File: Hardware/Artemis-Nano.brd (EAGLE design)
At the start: 43.2 x 20.3 mm, 129 parts, among them J10 USB-C, J11 CORTEX_DEBUG, U2 MCP73831, U3 3.3V, U4 ARTEMIS_MODULESMD, U6 CH340E_MSOP10, Y2 32.768kHz

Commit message: Rename to Nano. Add ignore. Add panel.
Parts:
- removed LOGO2: OSHW-LOGOS, SparkFun-Aesthetics:OSHW-LOGO-S
- removed LOGO3: SFE_LOGO_NAME_FLAME.1_INCH, SparkFun-Aesthetics:SFE_LOGO_NAME_FLAME_.1
- added U$25: (no value), SparkFun-Aesthetics:PRODUCTION_INSTRUCTIONS
- moved FRAME2 55.3 mm to (0.00, 0.00)
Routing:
- net 3.3V: track 50.7 -> 46.9 mm
- net GND: track 31.5 -> 28.7 mm
- added copper zone on layer 15, net 3.3V
- added copper zone on layer 2, net GND
- removed copper zone on layer 2, net 3.3V
- removed copper zone on layer 15, net GND
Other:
- board text added: "0.8mm Thickness"
- board text added: "Four-layer board"

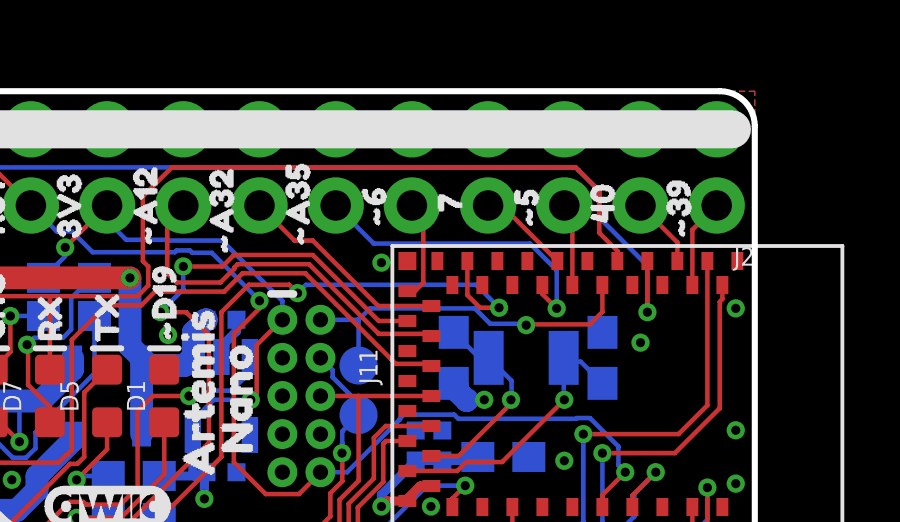
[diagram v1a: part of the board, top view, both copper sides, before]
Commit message: Fixing PWM pin 7. Updating schematic symbol.
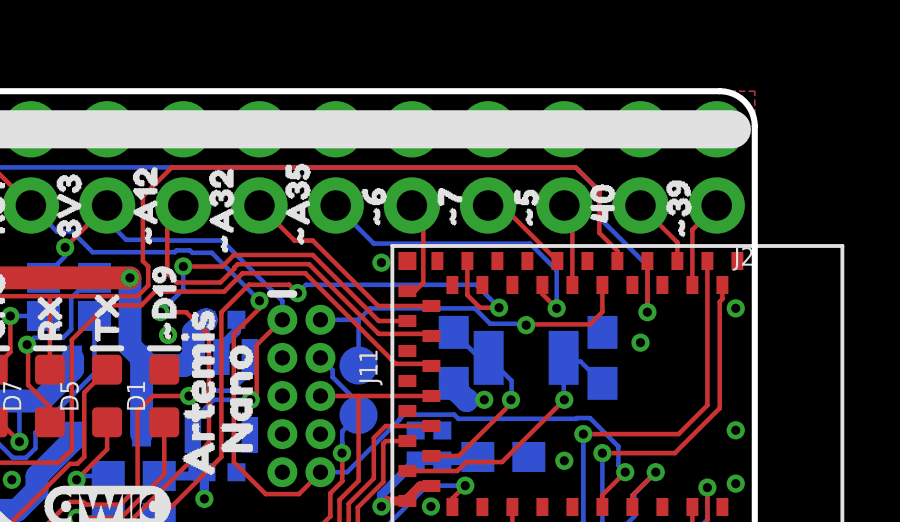
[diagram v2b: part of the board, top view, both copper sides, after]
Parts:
- removed U$20, U$79: (no value), buzzard_labels (10):78
- added U$32, U$34: (no value), buzzard_labels (1):#71
- moved U$19 0.25 mm to (36.2, 15.4)
- renumbered U4 to U1
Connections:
- net D7/MOSI renamed ~D7/MOSI

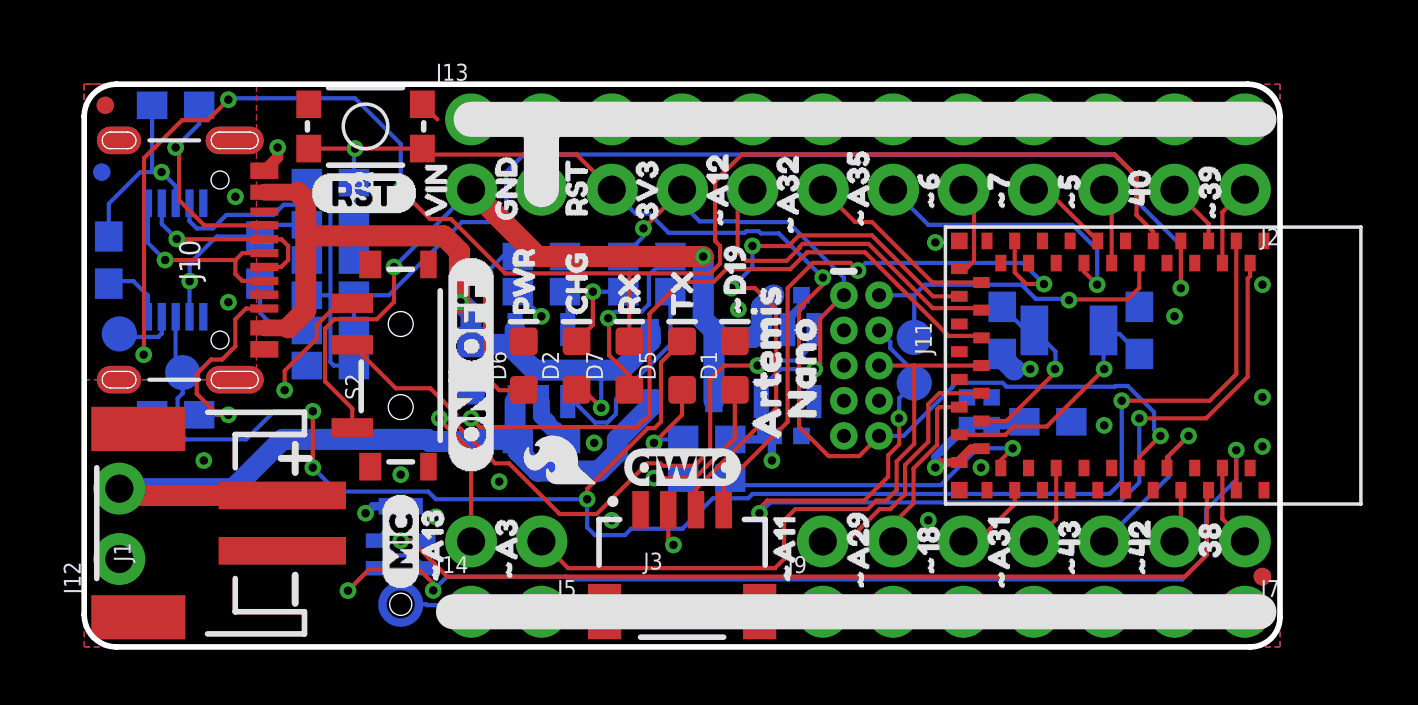
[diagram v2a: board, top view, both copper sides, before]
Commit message: Fix pin 33 silk
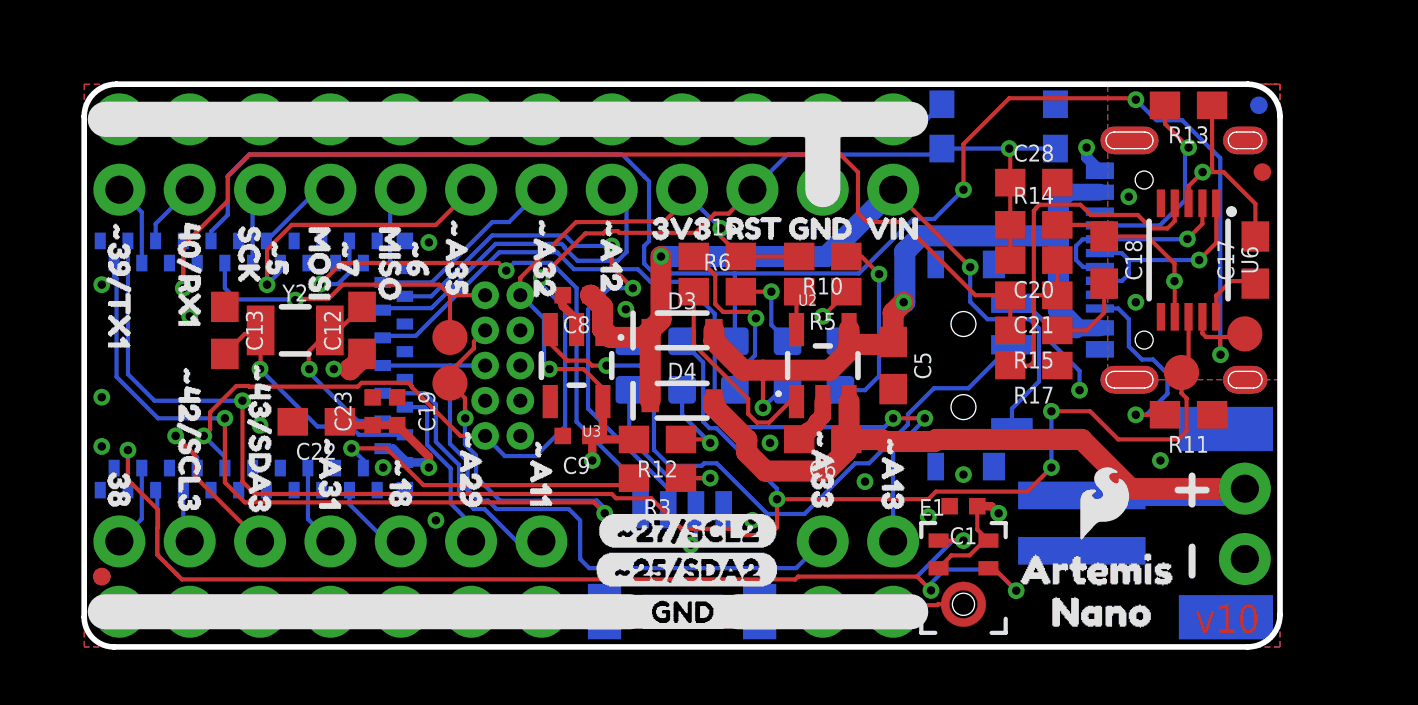
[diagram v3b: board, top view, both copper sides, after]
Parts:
- removed U$69, U$70: (no value), buzzard_labels (10):#A320
- added U$20, U$36: (no value), buzzard_labels (4):#A331
- moved U$25 55.9 mm to (-6.35, 50.8), flipped to the bottom
- moved FRAME2 43.2 mm to (43.2, 0.00), flipped to the top
- moved FD1 41.9 mm to (0.64, 2.54), flipped to the bottom
- moved FD3 41.9 mm to (42.5, 17.1), flipped to the top
- moved FD4 41.9 mm to (0.64, 2.54), flipped to the top
- moved FD2 41.7 mm to (42.4, 19.6), flipped to the bottom
- moved C17 41.4 mm to (42.3, 14.0), flipped to the top
- moved J12 40.6 mm to (41.9, 3.17), flipped to the bottom
- moved J2 40.6 mm to (1.27, 16.5), flipped to the bottom
- moved J7 40.6 mm to (1.27, 3.81), flipped to the bottom
- moved TP6 40.6 mm to (41.9, 11.3), flipped to the top
- moved U$31 40.6 mm to (1.27, 6.99), flipped to the top
- moved U$48 40.6 mm to (1.27, 16.0), flipped to the top
- moved FRAME1 38.1 mm to (40.6, -21.6), flipped to the bottom
- moved U$62 38.1 mm to (2.54, 14.7), flipped to the bottom
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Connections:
- net ~AD3/SWO renamed ~AD33/SWO
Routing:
- net PDMDATA: track 33.2 -> 6.59 mm
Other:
- outline, holes or cut-outs redrawn

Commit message: Fix pin 33 silk
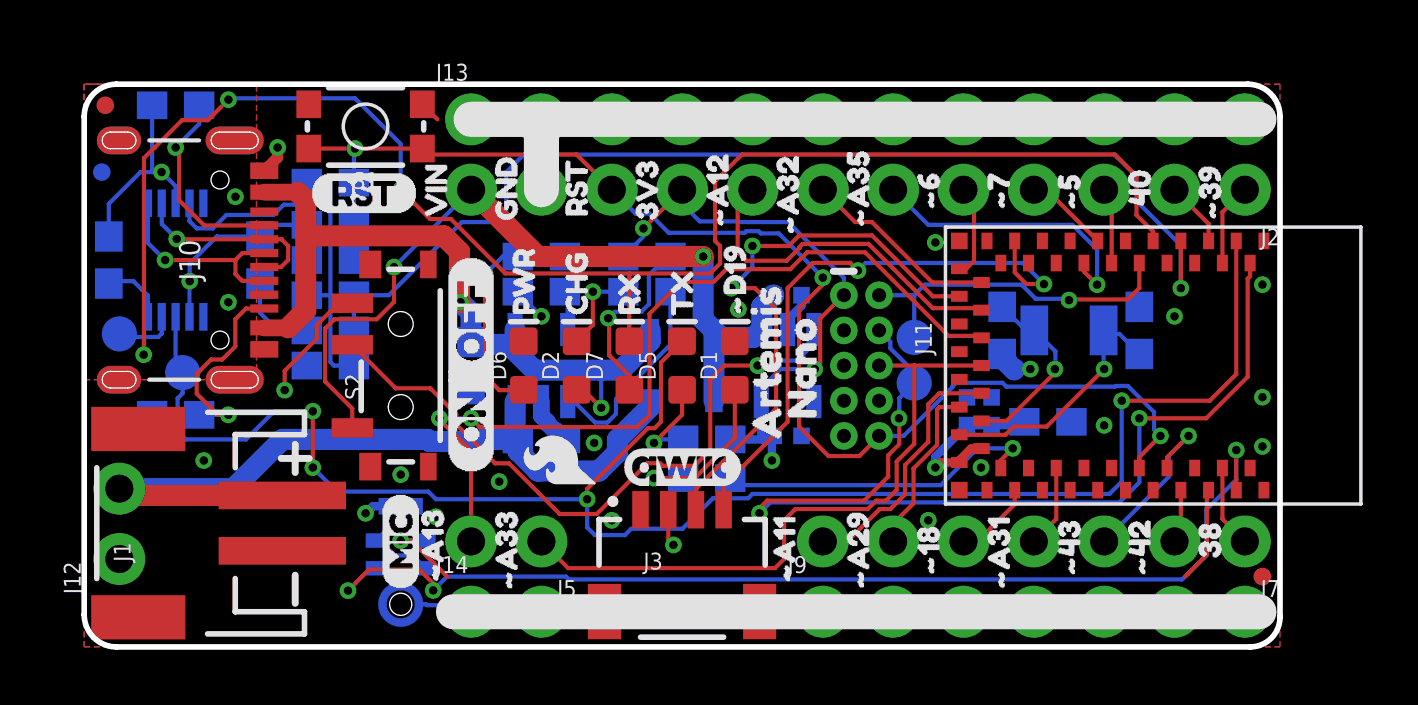
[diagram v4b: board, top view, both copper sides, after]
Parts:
- moved U$25 55.9 mm to (49.5, 50.8), flipped to the top
- moved FRAME2 43.2 mm to (0.00, 0.00), flipped to the bottom
- moved FD1 41.9 mm to (42.5, 2.54), flipped to the top
- moved FD3 41.9 mm to (0.64, 17.1), flipped to the bottom
- moved FD4 41.9 mm to (42.5, 2.54), flipped to the bottom
- moved FD2 41.7 mm to (0.76, 19.6), flipped to the top
- moved C17 41.4 mm to (0.89, 14.0), flipped to the bottom
- moved J12 40.6 mm to (1.27, 3.17), flipped to the top
- moved J2 40.6 mm to (41.9, 16.5), flipped to the top
- moved J7 40.6 mm to (41.9, 3.81), flipped to the top
- moved TP6 40.6 mm to (1.27, 11.3), flipped to the bottom
- moved U$31 40.6 mm to (41.9, 6.99), flipped to the bottom
- moved U$48 40.6 mm to (41.9, 16.0), flipped to the bottom
- moved FRAME1 38.1 mm to (2.54, -21.6), flipped to the top
- moved U$62 38.1 mm to (40.6, 14.7), flipped to the top
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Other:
- outline, holes or cut-outs redrawn

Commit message: Change silk to match new variant
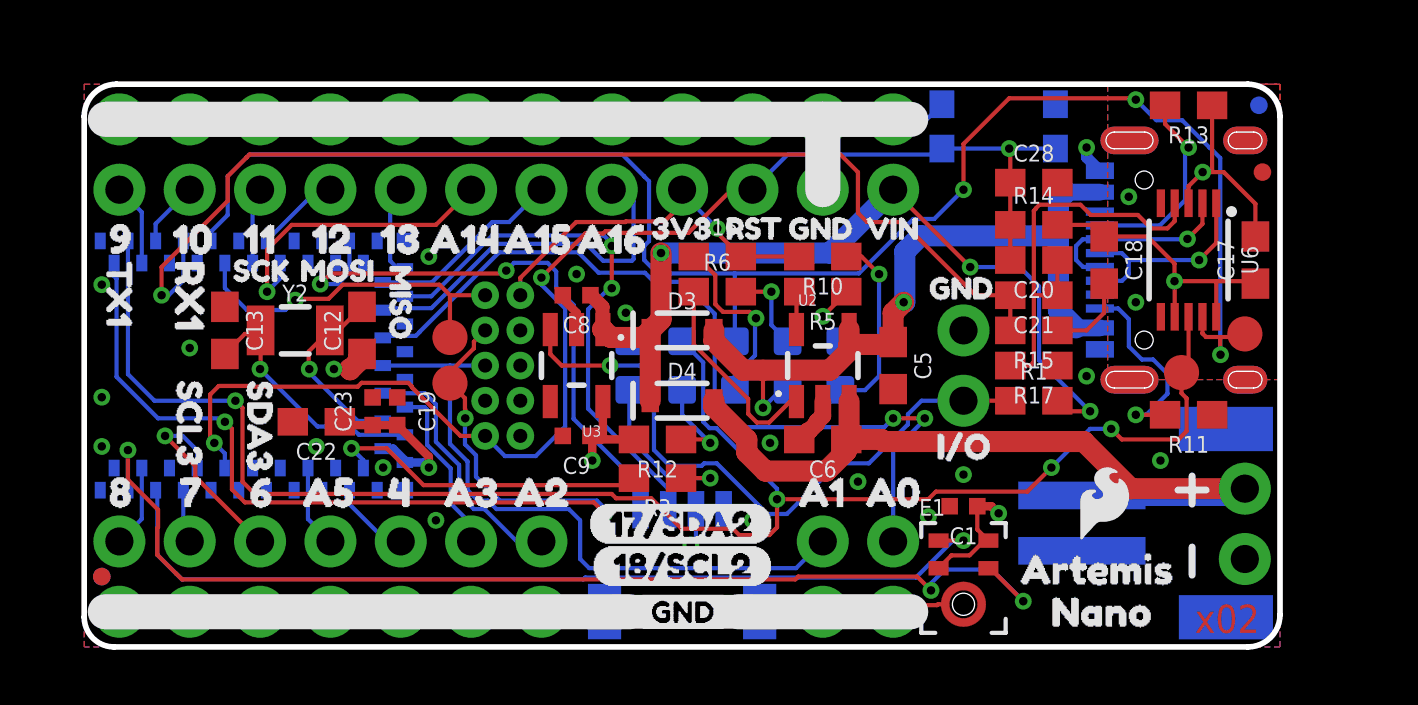
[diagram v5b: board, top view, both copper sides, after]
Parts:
- removed S2: (no value), SparkFun-Switches:SWITCH_SPST_SMD_A
- removed U$58: (no value), buzzard_labels:OFF2
- removed U$61: (no value), buzzard_labels (10):#66
- removed U$62: (no value), buzzard_labels (10):#394
- removed U$63: (no value), buzzard_labels (10):#510
- removed U$64, U$65: (no value), buzzard_labels (10):#1818
- removed U$66: (no value), buzzard_labels (10):#4213
- removed U$67: (no value), buzzard_labels (10):#4315
- removed U$68: (no value), buzzard_labels (10):#A120
- removed U$71, U$72: (no value), buzzard_labels (10):#A351
- removed U$73, U$74: (no value), buzzard_labels (10):#A1321
- removed U$75, U$76: (no value), buzzard_labels (10):#A2919
- removed U$78: (no value), buzzard_labels (10):40#RX12
- removed U$80: (no value), buzzard_labels (10):405
- removed U$81: (no value), buzzard_labels (10):3812
- added J4: (no value), SparkFun-Connectors:1X02_NO_SILK
- added R1: 10k, SparkFun-Resistors:0603
- added U$35: (no value), buzzard_labels:68
- added U$37: (no value), buzzard_labels:810
- added U$40: (no value), buzzard_labels:A10
- added U$41: (no value), buzzard_labels:A21
- added U$42: (no value), buzzard_labels:A32
- added U$43: (no value), buzzard_labels:GND17
- added U$45: (no value), buzzard_labels (1):90
- added U$46: (no value), buzzard_labels (1):101
- added U$47: (no value), buzzard_labels (1):112
- added U$52: (no value), buzzard_labels (1):123
- added U$53: (no value), buzzard_labels (1):134
- added U$54: (no value), buzzard_labels (1):A145
- added U$55: (no value), buzzard_labels (1):A156
- added U$56: (no value), buzzard_labels (1):A167
- U$10: device buzzard_labels (11):#A312 -> buzzard_labels:A57
- U$11: device buzzard_labels (11):#A321 -> buzzard_labels (2):SCL30
- U$12: device buzzard_labels (11):#A321 -> buzzard_labels (1):A145
- U$19: device buzzard_labels (10):#510 -> buzzard_labels:A32
- U$20: device buzzard_labels (4):#A331 -> buzzard_labels (16):A00
- U$21: device buzzard_labels (10):#66 -> buzzard_labels:A21
- U$23: device buzzard_labels (14):#D190 -> buzzard_labels (7):I#O3
- U$26: device buzzard_labels (16):#25#SDA21 -> buzzard_labels (6):191
- U$28: device buzzard_labels (10):#A120 -> buzzard_labels (1):A156
- U$29: device buzzard_labels (16):#27#SCL20 -> buzzard_labels:GND17
- U$31: device buzzard_labels (10):3812 -> buzzard_labels (2):SDA31
- U$32: device buzzard_labels (1):#71 -> buzzard_labels:46
- U$34: device buzzard_labels (1):#71 -> buzzard_labels:A10
- U$36: device buzzard_labels (4):#A331 -> buzzard_labels:79
- U$4: device buzzard_labels:ON1 -> buzzard_labels (7):I#O3
- U$48: device buzzard_labels (10):#39#TX13 -> buzzard_labels (1):A167
- U$50: device buzzard_labels (8):#A112 -> buzzard_labels (3):RX10
- U$57: device buzzard_labels (10):#42#SCL314 -> buzzard_labels (5):17#SDA21
- U$59: device buzzard_labels (8):#A112 -> buzzard_labels (2):TX12
- U$60: device buzzard_labels (10):#43#SDA316 -> buzzard_labels (5):18#SCL20
- U$9: device buzzard_labels (11):#A312 -> buzzard_labels (16):A00
- moved U$25 55.9 mm to (-6.35, 50.8), flipped to the bottom
- moved FRAME2 43.2 mm to (43.2, 0.00), flipped to the top
- moved FD1 41.9 mm to (0.64, 2.54), flipped to the bottom
- moved FD3 41.9 mm to (42.5, 17.1), flipped to the top
- moved FD4 41.9 mm to (0.64, 2.54), flipped to the top
- moved FD2 41.7 mm to (42.4, 19.6), flipped to the bottom
- moved C17 41.4 mm to (42.3, 14.0), flipped to the top
- moved J12 40.6 mm to (41.9, 3.17), flipped to the bottom
- moved J2 40.6 mm to (1.27, 16.5), flipped to the bottom
- moved J7 40.6 mm to (1.27, 3.81), flipped to the bottom
- moved TP6 40.6 mm to (41.9, 11.3), flipped to the top
- moved FRAME1 38.1 mm to (40.6, -21.6), flipped to the bottom
- moved R11 36.6 mm to (39.9, 8.38), flipped to the top
- moved R13 36.6 mm to (39.9, 19.6), flipped to the top
- moved U6 36.6 mm to (39.9, 14.0), flipped to the top
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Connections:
- net D38 renamed 8
- net D40/RX1 renamed 10
- net ~AD11 renamed ~A2
- net ~AD12 renamed ~A16
- net ~AD13 renamed ~A0
- net ~AD29 renamed ~A3
- net ~AD31 renamed ~A5
- net ~AD32 renamed ~A15
- net ~AD33/SWO renamed ~A1
- net ~AD35 renamed ~A14
- net ~D18 renamed ~4
- net ~D39/TX1 renamed ~9
- net ~D42 renamed ~7
- net ~D43 renamed ~6
- net ~D5/SCK renamed ~11
- net ~D6/MISO renamed ~13
- net ~D7/MOSI renamed ~12
- removed net N$6: C17.1, U6.10
- net 3.3V: now also C17.1, U6.10
- net GND: now also J4.2; no longer S2.1
- net VIN: now also R1.2; no longer S2.3
- net VREG_EN: now also J4.1, R1.1; no longer S2.2
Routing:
- net PDMDATA: track 6.59 -> 33.3 mm
- net GND: track 28.7 -> 24.2 mm, vias 20 -> 21
- net N$6: track 2.43 -> 0.00 mm
- net RXI-0: track 62.9 -> 61.1 mm
- net VIN: track 30.2 -> 31.5 mm, vias 2 -> 3
- net BOOT: track 39.2 -> 40.5 mm
- net 3.3V: track 46.9 -> 45.8 mm, vias 7 -> 6
- net ~D25/SDA2: track 20.7 -> 19.7 mm
- net PDMCLK: track 39.4 -> 40.3 mm
- net ~A16: track 12.7 -> 13.4 mm
- net ~6: track 6.55 -> 7.24 mm
- net VREG_EN: track 24.0 -> 23.4 mm
- net ~A14: track 10.5 -> 11.0 mm
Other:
- outline, holes or cut-outs redrawn
- board text added: "x02"
- board text removed: "v10"

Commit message: Fixed TX/RX LED label swap
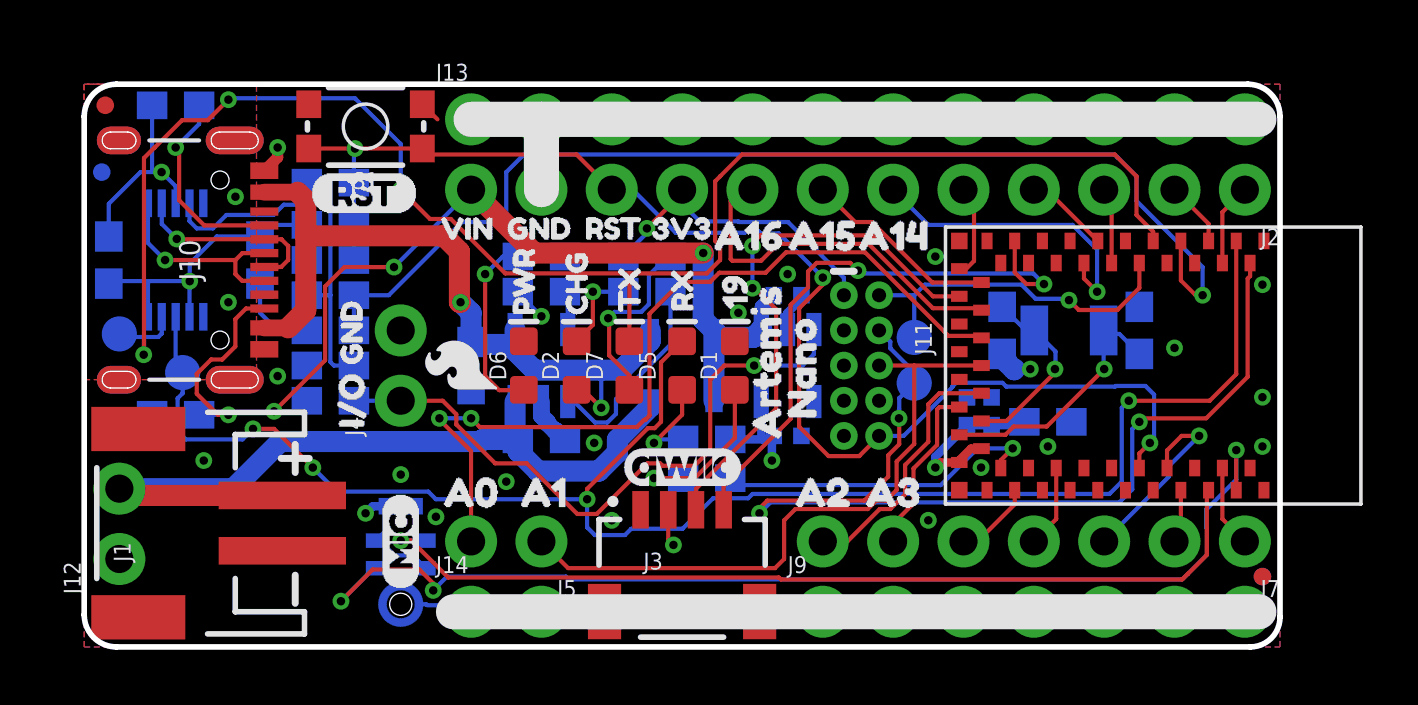
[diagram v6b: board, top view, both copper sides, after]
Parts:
- moved U$25 55.9 mm to (49.5, 50.8), flipped to the top
- moved FRAME2 43.2 mm to (0.00, 0.00), flipped to the bottom
- moved U$37 43.2 mm to (43.2, 5.59), flipped to the bottom
- moved U$45 43.2 mm to (43.2, 14.7), flipped to the bottom
- moved FD1 41.9 mm to (42.5, 2.54), flipped to the top
- moved FD3 41.9 mm to (0.64, 17.1), flipped to the bottom
- moved FD4 41.9 mm to (42.5, 2.54), flipped to the bottom
- moved FD2 41.7 mm to (0.76, 19.6), flipped to the top
- moved C17 41.4 mm to (0.89, 14.0), flipped to the bottom
- moved J12 40.6 mm to (1.27, 3.17), flipped to the top
- moved J2 40.6 mm to (41.9, 16.5), flipped to the top
- moved J7 40.6 mm to (41.9, 3.81), flipped to the top
- moved TP6 40.6 mm to (1.27, 11.3), flipped to the bottom
- moved U$59 40.6 mm to (41.9, 14.9), flipped to the bottom
- moved U$46 38.6 mm to (40.9, 14.7), flipped to the bottom
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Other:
- outline, holes or cut-outs redrawn
